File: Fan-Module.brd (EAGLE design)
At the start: 58 x 66 mm, 15 parts

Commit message: added sdi functionality to fan module
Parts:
- removed C2: 47uF, SparkFun-Capacitors:PANASONIC_D
- removed D2: 3A/40V/500mV, SparkFun-DiscreteSemi:SMA-DIODE
- removed U$2: M20-8900505, MESO:M20-8900505
- added C1: (no value), rcl:C0603
- added C4, C5: 10uF, rcl:C0603
- added D3: 3A/40V/500mV, SparkFun-DiscreteSemi:SMA-DIODE
- added F1: (no value), adafruit:1812
- added J1: (no value), SparkFun-Connectors:USB-B-MICRO-SMD
- added J10: (no value), SparkFun-Connectors:1X02_LONGPADS
- added J2: (no value), SparkFun-Connectors:1X05
- added LED1: (no value), led:CHIPLED_0805
- added Q1: (no value), microbuilder:SOT23-WIDE
- added R1, R2: 2k, rcl:R1206
- added R6: 59R, rcl:R0805
- added U1: ATSAMD11C14A-SSUT_ATSAMD11C14A-SSUT, LED-Board:ATSAMD11C14A-SSUT_SOIC127P600X160-14N
- added U3: LDL1117S12R_LDL1117S12R, LDL1117S12R:LDL1117S12R_SOT230P700X180-4N
- moved D1 38.9 mm to (12.8, 32.2), turned to 270 degrees
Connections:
- removed net 24V: D2.C, U$2.5
- removed net FAN-VCC: C2.+, D1.C, U$2.1
- removed net PWM: D1.A, PWM-CLIP.CLIP-INPUT1, PWM-CLIP.CLIP-INPUT2, PWM-CLIP1.CLIP-INPUT1, PWM-CLIP1.CLIP-INPUT2
- new net 3.3V: C1.2, C4.2, J2.2, R6.2, U1.12, U3.2, U3.4
- new net BUS: PWM-CLIP.CLIP-INPUT1, PWM-CLIP.CLIP-INPUT2, PWM-CLIP1.CLIP-INPUT1, PWM-CLIP1.CLIP-INPUT2, R1.1
- new net FAN: J10.2, Q1.3
- new net N$1: LED1.C, U1.14
- new net N$2: LED1.A, R6.1
- new net N$3: R1.2, U1.5
- new net N$4: D3.A, J1.VBUS
- new net N$5: Q1.1, R2.2, U1.13
- new net N$6: D1.A, F1.1
- new net RESET: J2.5, U1.6
- new net SWCLK: J2.4, U1.7
- new net SWDIO: J2.3, U1.8
- new net USB+: J1.D+, U1.10
- new net USB-: J1.D-, U1.9
- new net VCC: C5.2, D1.C, D3.C, J10.1, U3.3
- net GND: now also C1.1, C4.1, C5.1, J1.GND, J1.SHIELD1, J1.SHIELD2, J1.SHIELD3, J2.1, Q1.2, R2.1, U1.11, U3.1; no longer C2.-, U$2.3
- net VCC-RAW: now also F1.2; no longer D2.A
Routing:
- net VCC-RAW: track 142.5 -> 16.5 mm, vias 0 -> 1
- net 3.3V: track 0.00 -> 60.8 mm, vias 0 -> 2
- net N$5: track 0.00 -> 60.3 mm
- net BUS: track 0.00 -> 52.5 mm
- net N$3: track 0.00 -> 45.3 mm
- net SWDIO: track 0.00 -> 33.5 mm, vias 0 -> 1
- net RESET: track 0.00 -> 32.9 mm, vias 0 -> 1
- net VCC: track 0.00 -> 30.7 mm, vias 0 -> 3
- net SWCLK: track 0.00 -> 28.9 mm, vias 0 -> 1
- net USB+: track 0.00 -> 24.0 mm
- net USB-: track 0.00 -> 23.8 mm
- net FAN-VCC: track 23.0 -> 0.00 mm
- net PWM: track 22.2 -> 0.00 mm
- net GND: track 0.00 -> 22.0 mm, vias 0 -> 2
- net N$4: track 0.00 -> 16.0 mm
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- added copper zone on layer 16, net BUS
- removed copper zone on layer 16, net PWM
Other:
- board text added: "BUS"
- board text removed: "LED+"
- board text removed: "LED-"
- board text removed: "PWM"

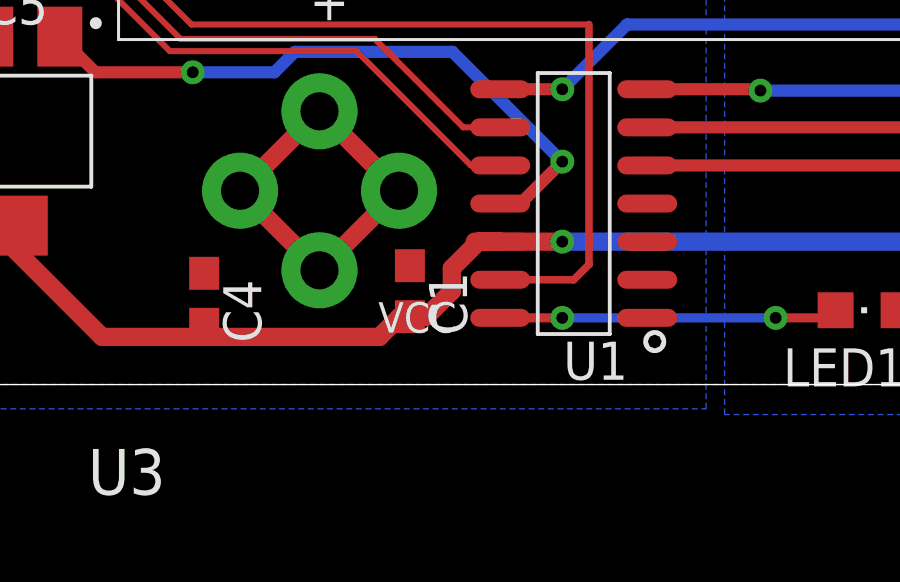
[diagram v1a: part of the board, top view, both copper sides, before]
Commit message: modified c6 to 1uF
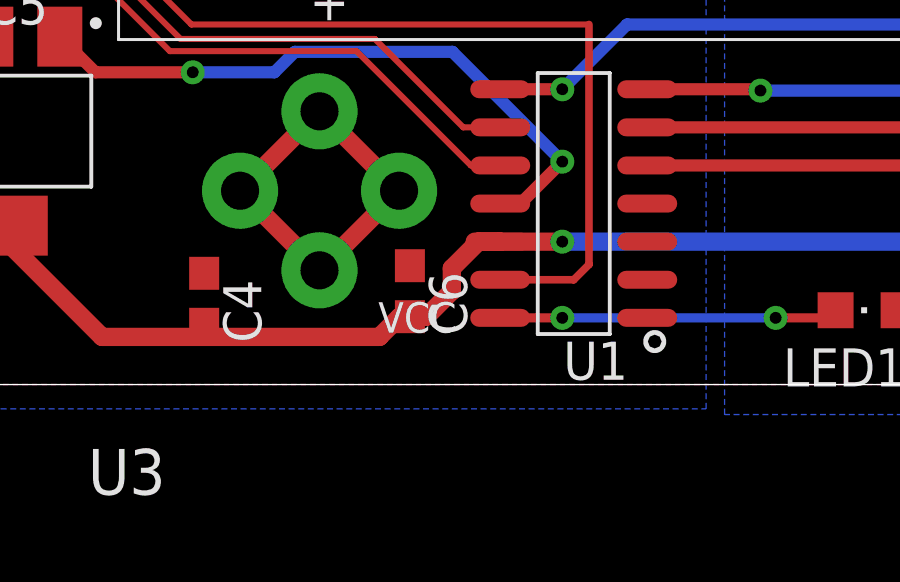
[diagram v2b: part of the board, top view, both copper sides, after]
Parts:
- C6: value (none) -> 1uF
- renumbered C1 to C6
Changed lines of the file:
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@@
 <drawing>
 <settings>
-<setting alwaysvectorfont="yes"/>
+<setting alwaysvectorfont="no"/>
 <setting keepoldvectorfont="yes"/>
 <setting verticaltext="up"/>
@@
 <attribute name="VALUE" x="41.021" y="9.017" size="1.27" layer="27" rot="R180"/>
 </element>
-<element name="C1" library="rcl" library_urn="urn:adsk.eagle:library:334" package="C0603" package3d_urn="urn:adsk.eagle:package:23616/2" value="" x="24.511" y="7.112" smashed="yes" rot="R270">
+<element name="C6" library="rcl" library_urn="urn:adsk.eagle:library:334" package="C0603" package3d_urn="urn:adsk.eagle:package:23616/2" value="1uF" x="24.511" y="7.112" smashed="yes" rot="R270">
 <attribute name="NAME" x="25.146" y="7.747" size="1.27" layer="25" rot="R270"/>
 <attribute name="SPICEPREFIX" value="C" x="24.511" y="7.112" size="1.778" layer="27" rot="R270" display="off"/>
@@
 </polygon>
 <contactref element="J1" pad="GND"/>
-<contactref element="C1" pad="1"/>
+<contactref element="C6" pad="1"/>
 <contactref element="J1" pad="SHIELD2"/>
 <contactref element="J1" pad="SHIELD1"/>
@@
 </signal>
 <signal name="3.3V">
-<contactref element="C1" pad="2"/>
+<contactref element="C6" pad="2"/>
 <contactref element="R6" pad="2"/>
 <contactref element="J2" pad="2"/>
